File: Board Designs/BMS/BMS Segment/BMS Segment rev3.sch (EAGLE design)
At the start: 117 parts

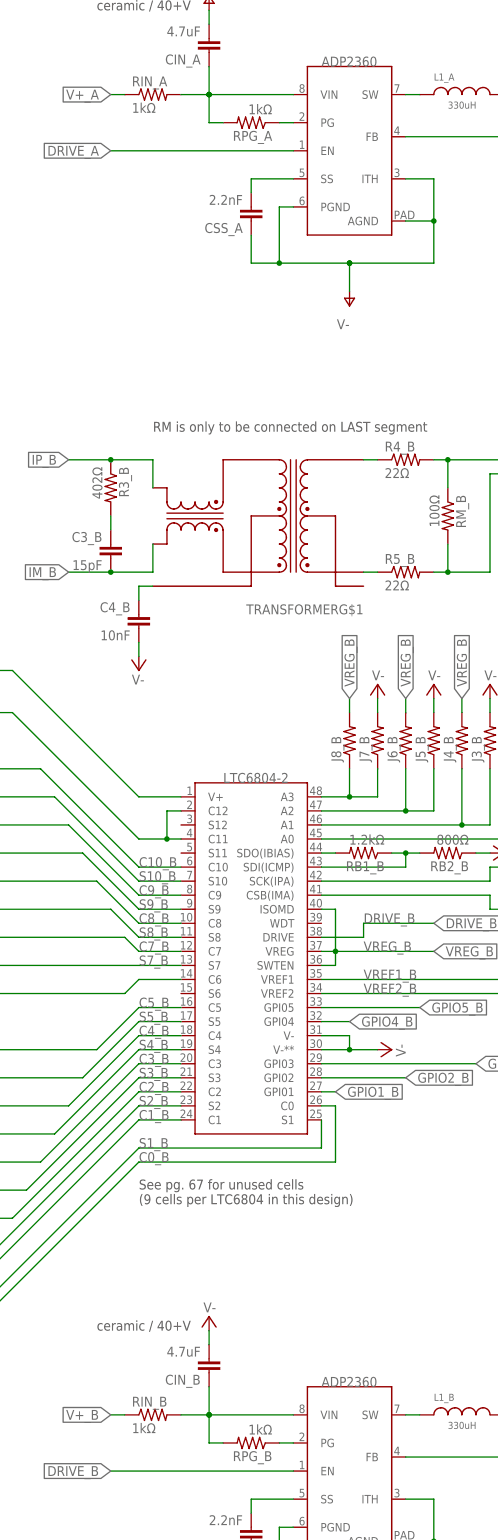
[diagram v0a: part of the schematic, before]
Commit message: BMS Segments: Change pull-up resistor value on ADP2360 voltage regulator to 10Mohm from 1kohm, fixing sleep-mode current drain bug
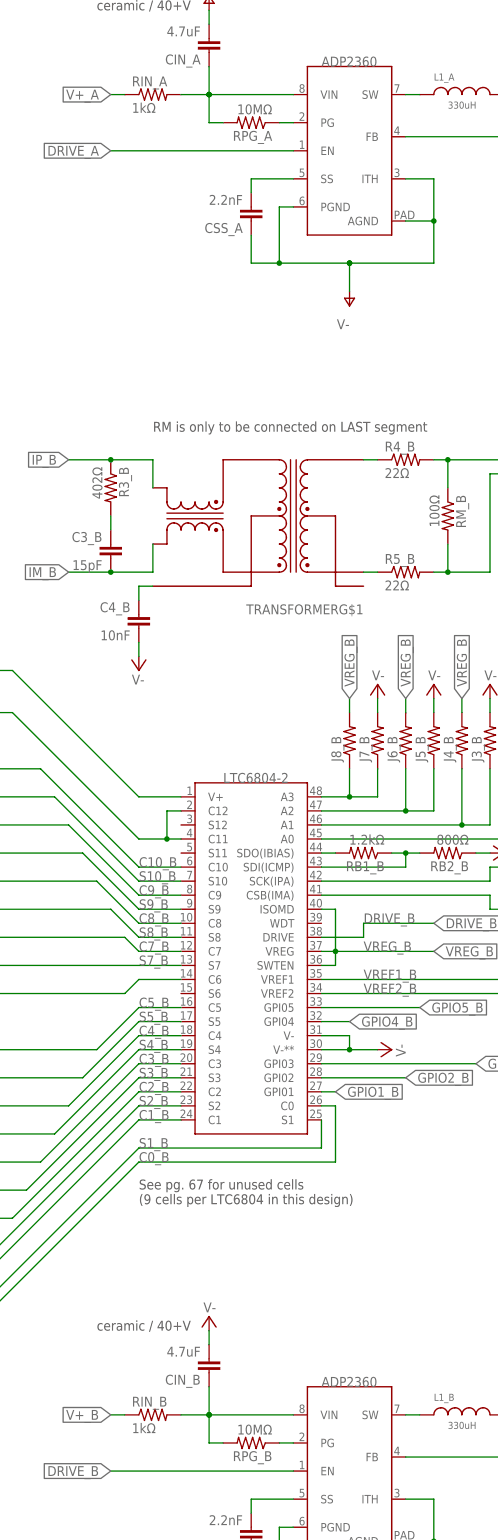
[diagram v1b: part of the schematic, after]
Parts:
- RPG_A, RPG_B: value 1kΩ -> 10MΩ
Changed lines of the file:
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@@
 <part name="CIN_B" library="HyTechDevices" deviceset="CAP" device="0805" value="4.7uF"/>
 <part name="SUPPLY2" library="supply2" deviceset="V-" device=""/>
-<part name="RPG_B" library="HyTechDevices" deviceset="RESISTOR" device="0805-RES" value="1kΩ"/>
+<part name="RPG_B" library="HyTechDevices" deviceset="RESISTOR" device="0805-RES" value="10MΩ"/>
 <part name="SUPPLY12" library="supply2" deviceset="V-" device=""/>
 <part name="CSS_B" library="HyTechDevices" deviceset="CAP" device="0805" value="2.2nF"/>
@@
 <part name="CIN_A" library="HyTechDevices" deviceset="CAP" device="0805" value="4.7uF"/>
 <part name="SUPPLY40" library="supply1" deviceset="V-" device=""/>
-<part name="RPG_A" library="HyTechDevices" deviceset="RESISTOR" device="0805-RES" value="1kΩ"/>
+<part name="RPG_A" library="HyTechDevices" deviceset="RESISTOR" device="0805-RES" value="10MΩ"/>
 <part name="SUPPLY41" library="supply1" deviceset="V-" device=""/>
 <part name="CSS_A" library="HyTechDevices" deviceset="CAP" device="0805" value="2.2nF"/>
